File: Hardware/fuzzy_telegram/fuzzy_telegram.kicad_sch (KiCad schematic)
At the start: 1 part, among them U1 STM32MP157DAB1

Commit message: start on DDR3L schematic
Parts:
- added R2: 240, symbol Device:R_Small
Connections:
- net DDR_DQ0: now reaches U1.A17 (DDR_DQ0)
- net DDR_DQ1: now reaches U1.A18 (DDR_DQ1)
- net DDR_DQ3: now reaches U1.B17 (DDR_DQ3)
- net DDR_DQ7: now reaches U1.B18 (DDR_DQ7)
- net DDR_~{DQSL}: now reaches U1.B19 (DDR_DQS0N)
- net DDR_DQML: now reaches U1.C18 (DDR_DQM0)
- net DDR_DQSL: now reaches U1.C19 (DDR_DQS0P)
- net DDR_DQ5: now reaches U1.D17 (DDR_DQ5)
- net DDR_DQ2: now reaches U1.D18 (DDR_DQ2)
- net DDR_DQ6: now reaches U1.D19 (DDR_DQ6)
- net DDR_A7: now reaches U1.E17 (DDR_A7)
- net DDR_DQ4: now reaches U1.E18 (DDR_DQ4)
- net DDR_A13: now reaches U1.F17 (DDR_A13)
- net at U1.F18 (DDR_ZQ): now also R2.1
- net DDR_A3: now reaches U1.F19 (DDR_A3)
- net DDR_~{RST}: now reaches U1.G16 (DDR_RESETN)
- net DDR_A9: now reaches U1.G17 (DDR_A9)
- net DDR_A2: now reaches U1.G18 (DDR_A2)
- net DDR_BA0: now reaches U1.G19 (DDR_BA0)
- net DDR_A5: now reaches U1.H17 (DDR_A5)
- net DDR_A0: now reaches U1.H18 (DDR_A0)
- net DDR_ODT: now reaches U1.H19 (DDR_ODT)
- net DDR_BA2: now reaches U1.J16 (DDR_BA2)
- net DDR_~{WE}: now reaches U1.J17 (DDR_WEN)
- net DDR_~{CS}: now reaches U1.J18 (DDR_CSN)
- net DDR_~{CAS}: now reaches U1.K17 (DDR_CASN)
- net DDR_~{CLK}: now reaches U1.K19 (DDR_CLKN)
- net DDR_A12: now reaches U1.L17 (DDR_A12)
- net DDR_~{RAS}: now reaches U1.L18 (DDR_RASN)
- net DDR_CLK: now reaches U1.L19 (DDR_CLKP)
- net DDR_A1: now reaches U1.M17 (DDR_A1)
- net DDR_A11: now reaches U1.M18 (DDR_A11)
- net DDR_A10: now reaches U1.M19 (DDR_A10)
- net DDR_A6: now reaches U1.N16 (DDR_A6)
- net DDR_BA1: now reaches U1.N17 (DDR_BA1)
- net DDR_A14: now reaches U1.N18 (DDR_A14)
- net DDR_A4: now reaches U1.P17 (DDR_A4)
- net DDR_DQ8: now reaches U1.P18 (DDR_DQ8)
- net DDR_CKE: now reaches U1.P19 (DDR_CKE)
- net DDR_A8: now reaches U1.R17 (DDR_A8)
- net DDR_DQ10: now reaches U1.R18 (DDR_DQ10)
- net GND: now reaches U1.T15 (BYPASS_REG1V8)
- net GND: now also R2.2
- net DDR_DQ9: now reaches U1.T17 (DDR_DQ9)
- net DDR_DQ13: now reaches U1.T18 (DDR_DQ13)
- net DDR_~{DQSU}: now reaches U1.T19 (DDR_DQS1N)
- net DDR_DQMU: now reaches U1.U18 (DDR_DQM1)
- net DDR_DQSU: now reaches U1.U19 (DDR_DQS1P)
- net DDR_DQ14: now reaches U1.V18 (DDR_DQ14)
- net DDR_DQ11: now reaches U1.V19 (DDR_DQ11)
- net DDR_DQ15: now reaches U1.W17 (DDR_DQ15)
- net DDR_DQ12: now reaches U1.W18 (DDR_DQ12)
- no-connect marks 0 -> 1
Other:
- added sheet DDR (ddrf.kicad_sch)
- moved on the sheet: U1B, U1C

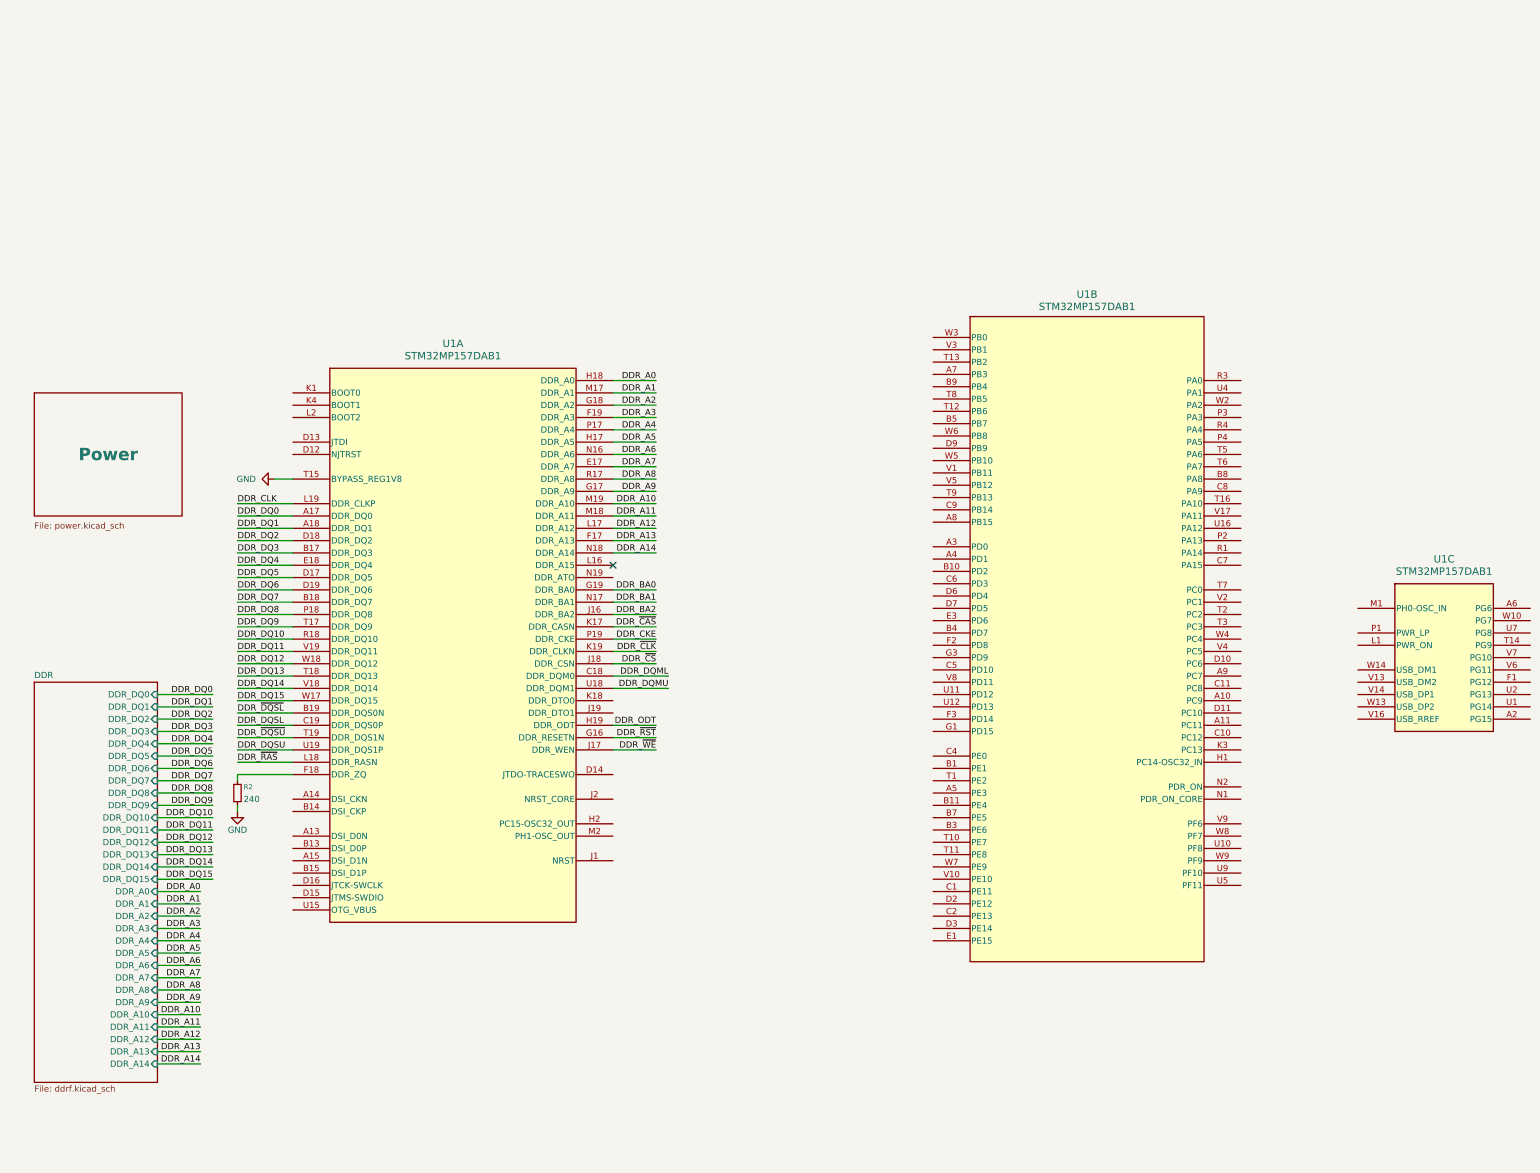
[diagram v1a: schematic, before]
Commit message: add SD card and more
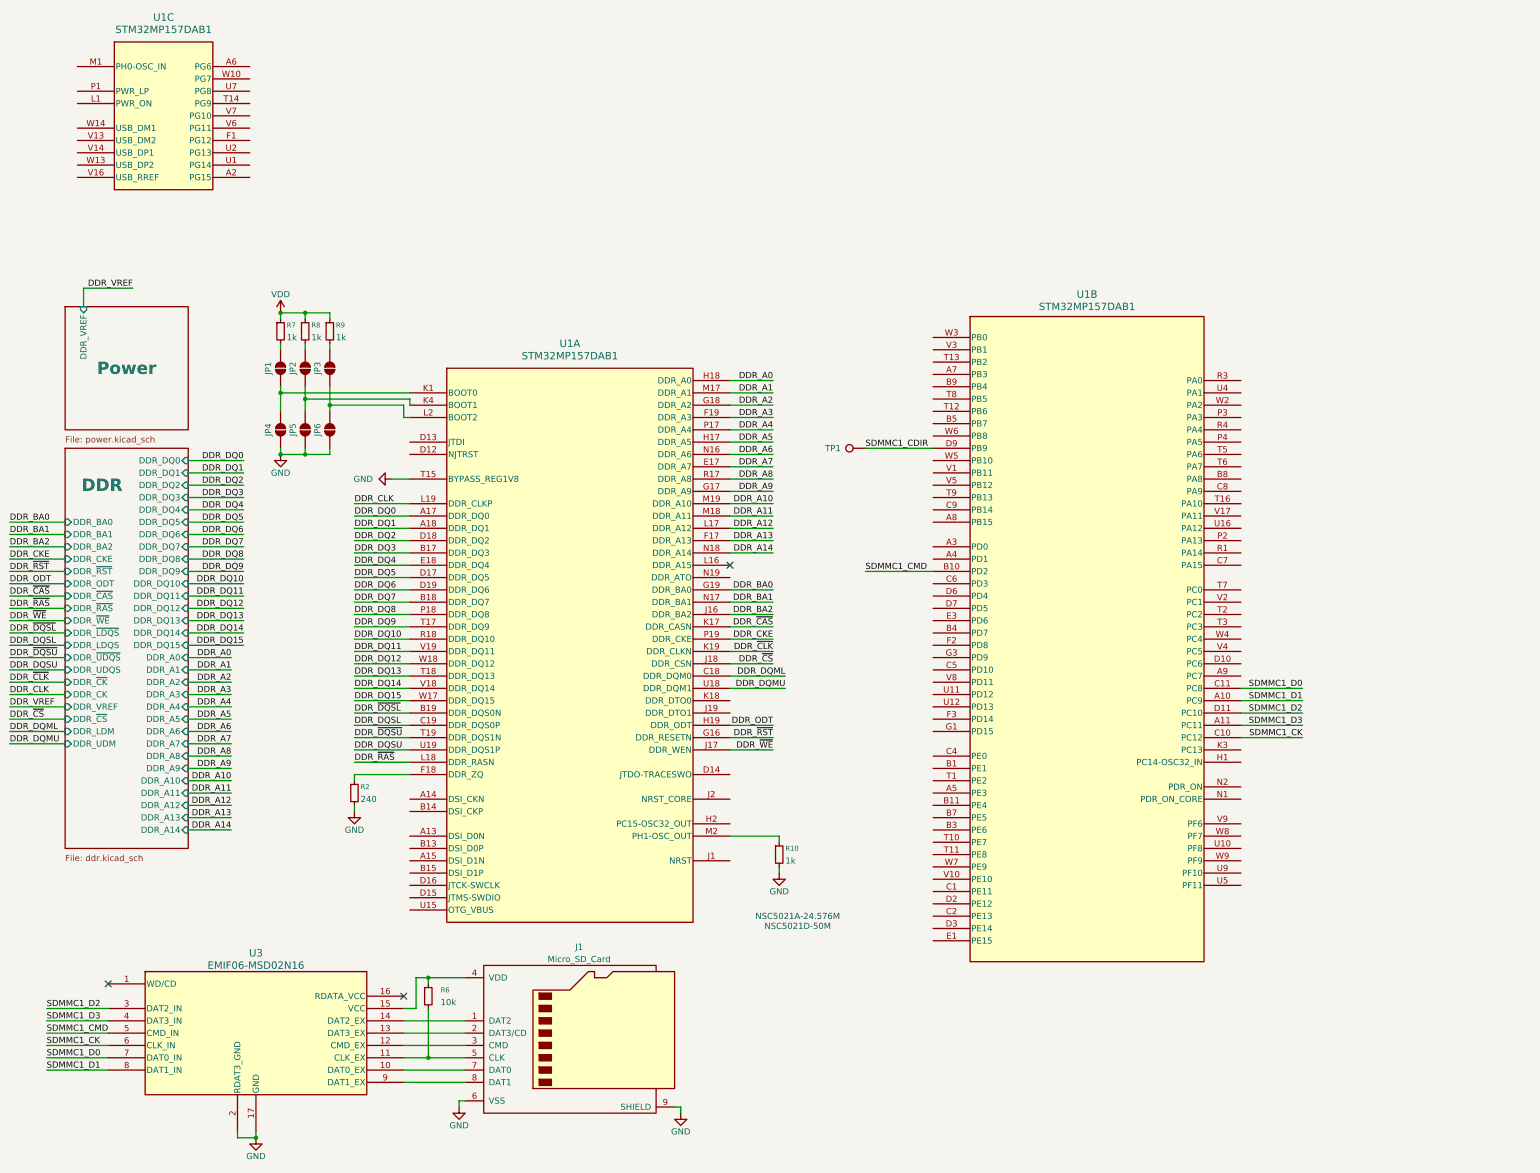
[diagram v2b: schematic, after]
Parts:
- added J1: Micro_SD_Card, symbol Connector:Micro_SD_Card
- added JP1, JP2, JP3, JP4, JP5, JP6: SolderJumper_2_Open, symbol Jumper:SolderJumper_2_Open
- added R10, R7, R8, R9: 1k, symbol Device:R_Small
- added R6: 10k, symbol Device:R_Small
- added TP1: TestPoint, symbol Connector:TestPoint
- added U3: EMIF06-MSD02N16, MICROQFN16_1P25X3P55X0P4_STM, symbol fuzzy_telegram:EMIF06-MSD02N16
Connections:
- net GND: now also J1.6 (VSS), J1.9 (SHIELD), JP4.1 (A), JP5.1 (A), JP6.1 (A), R10.2, U3.17 (GND), U3.2 (RDAT3_GND)
- net SDMMC1_D1: now reaches U1.A10 (PC9)
- net SDMMC1_D1: now also U3.8 (DAT1_IN)
- net SDMMC1_D3: now reaches U1.A11 (PC11)
- net SDMMC1_D3: now also U3.4 (DAT3_IN)
- net SDMMC1_CMD: now reaches U1.B10 (PD2)
- net SDMMC1_CMD: now also U3.5 (CMD_IN)
- net SDMMC1_CK: now reaches U1.C10 (PC12)
- net SDMMC1_CK: now also U3.6 (CLK_IN)
- net SDMMC1_D0: now reaches U1.C11 (PC8)
- net SDMMC1_D0: now also U3.7 (DAT0_IN)
- net SDMMC1_D2: now reaches U1.D11 (PC10)
- net SDMMC1_D2: now also U3.3 (DAT2_IN)
- net SDMMC1_CDIR: now reaches U1.D9 (PB9)
- net SDMMC1_CDIR: now also TP1.1
- net at U1.K1 (BOOT0): now also JP1.1 (A), JP4.2 (B)
- net at U1.K4 (BOOT1): now also JP2.1 (A), JP5.2 (B)
- net at U1.L2 (BOOT2): now also JP3.1 (A), JP6.2 (B)
- net at U1.M2 (PH1-OSC_OUT): now also R10.1
- new net: JP1.2 (B), R7.2
- new net: J1.1 (DAT2), U3.14 (DAT2_EX)
- new net: J1.2 (DAT3/CD), U3.13 (DAT3_EX)
- new net: J1.3 (CMD), U3.12 (CMD_EX)
- new net: J1.4 (VDD), R6.1, U3.15 (VCC)
- new net: J1.5 (CLK), R6.2, U3.11 (CLK_EX)
- new net: J1.7 (DAT0), U3.10 (DAT0_EX)
- new net: J1.8 (DAT1), U3.9 (DAT1_EX)
- new net: JP2.2 (B), R8.2
- new net: JP3.2 (B), R9.2
- new net VDD: R7.1, R8.1, R9.1
- no-connect marks 1 -> 3
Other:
- sheet DDR: file ddrf.kicad_sch -> ddr.kicad_sch
- sheet DDR ports: added DDR_BA0, DDR_BA1, DDR_BA2, DDR_CK, DDR_CKE, DDR_LDM, DDR_LDQS, DDR_ODT, DDR_UDM, DDR_UDQS, DDR_VREF, DDR_~{CAS}, DDR_~{CK}, DDR_~{CS}, DDR_~{LDQS}, DDR_~{RAS}, DDR_~{RST}, DDR_~{UDQS}, DDR_~{WE}; removed none
- sheet Power ports: added DDR_VREF; removed none
- note added: "NSC5021A-24.576M NSC5021D-50M"
- moved on the sheet: R2, U1A, U1C

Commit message: Started power design
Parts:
- added C44, C59: 10nF, symbol Device:C_Small
- added C60: C_Small, symbol Device:C_Small
- added R11: 10, symbol Device:R_Small
- added R12: 10k, symbol Device:R_Small
- added R15, R16: 0, symbol Device:R_Small
- added R21: 470k, symbol Device:R_Small
- added SW1: ~, symbol Switch:SW_SPST
- added U4: ~, Oscillator:Oscillator_SMD_SiT_PQFN-4Pin_2.0x1.6mm, symbol fuzzy_telegram:NSC5021D
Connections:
- net GND: now also C44.2, C59.2, R21.2, SW1.2 (B), U4.2 (GND)
- net VDD: now also R11.1
- net PWR_ON: now reaches U1.L1 (PWR_ON)
- net PWR_ON: now also R12.2, R15.2, R21.1
- net OSC_IN: now reaches U1.M1 (PH0-OSC_IN)
- net OSC_IN: now also U4.3 (OUTPUT)
- net NRST: now reaches U1.J1 (NRST)
- net NRST: now also C59.1, C60.2, R16.1, SW1.1 (A)
- net at U1.J2 (NRST_CORE): now also C60.1
- new net: R12.1, U4.1 (STANDBY)
- new net: C44.1, R11.2, U4.4 (Vcc)
- new net Power/1V35_EN: R15.1, R16.2
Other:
- sheet Power ports: added 1V2_EN, 1V35_EN; removed none
- moved on the sheet: JP1, JP2, JP3, JP4, JP5, JP6, R10, R7, R8, R9, U1C
